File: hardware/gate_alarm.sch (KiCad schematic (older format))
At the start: 8 parts, among them U1 ATtiny212-SS, U2 NodeMCU_1.0_(ESP-12E), U3 NCP718, U4 AH9250

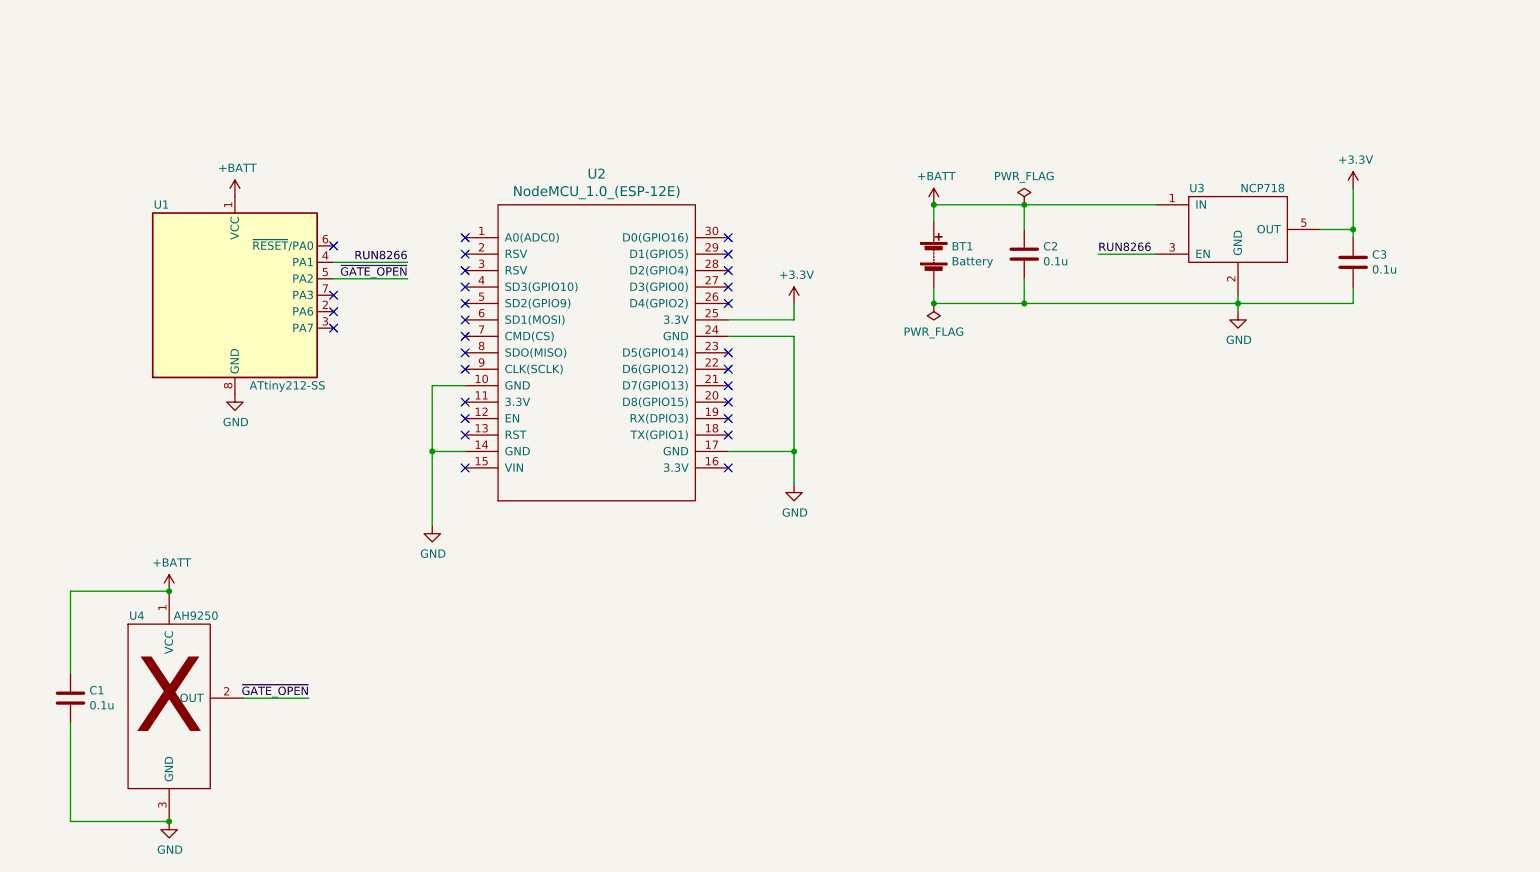
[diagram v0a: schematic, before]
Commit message: Update hardware for first PCB manufacture
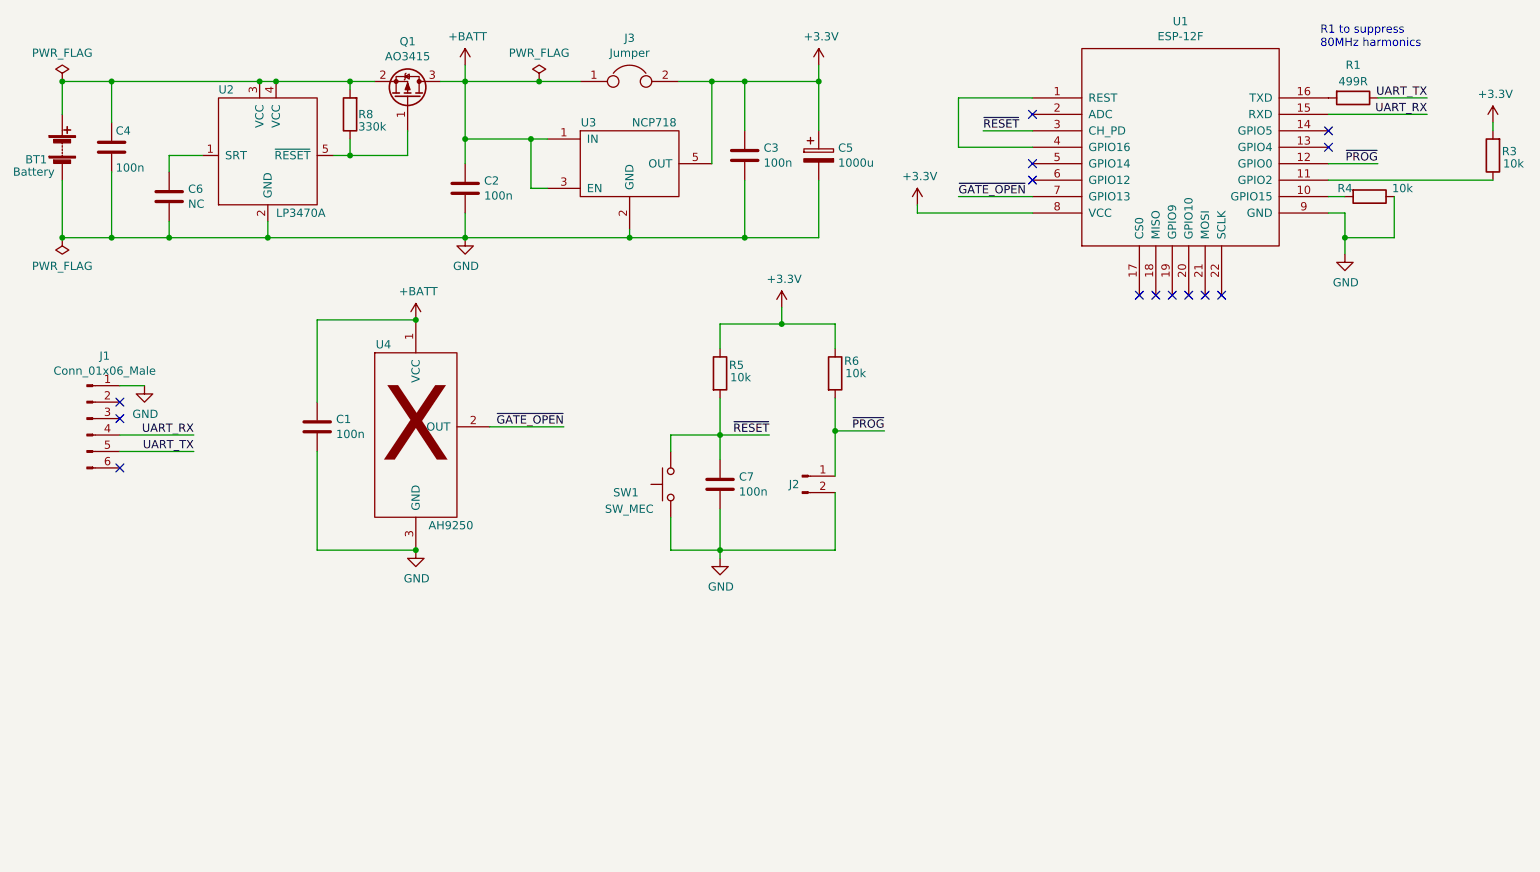
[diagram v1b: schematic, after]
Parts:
- removed U1: ATtiny212-SS, Package_SO:SOIC-8_3.9x4.9mm_P1.27mm, symbol MCU_Microchip_ATtiny:ATtiny212-SS
- removed U2: NodeMCU_1.0_(ESP-12E), ESP8266:NodeMCU1.0(12-E), symbol custom_symbols:NodeMCU_1.0_(ESP-12E)
- added C4, C7: 100n, Capacitors_SMD:C_0805_HandSoldering, symbol Device:C
- added C5: 1000u, Capacitors_THT:CP_Radial_D8.0mm_P3.50mm, symbol Device:CP
- added C6: NC, Capacitors_SMD:C_0805_HandSoldering, symbol Device:C
- added J1: Conn_01x06_Male, Pin_Headers:Pin_Header_Straight_1x06_Pitch2.54mm, symbol Connector:Conn_01x06_Male
- added J2: Conn_01x02_Male, Pin_Headers:Pin_Header_Straight_1x02_Pitch2.54mm, symbol Connector:Conn_01x02_Male
- added J3: Jumper, Jumpers:SolderJumper-2_P1.3mm_Open_Pad1.0x1.5mm, symbol Device:Jumper
- added Q1: AO3415, TO_SOT_Packages_SMD:SOT-23_Handsoldering, symbol Device:Q_PMOS_GSD
- added R1: 499R, Resistors_SMD:R_0805_HandSoldering, symbol Device:R
- added R3, R4, R5, R6: 10k, Resistors_SMD:R_0805_HandSoldering, symbol Device:R
- added R8: 330k, Resistors_SMD:R_0805_HandSoldering, symbol Device:R
- added SW1: SW_MEC, custom_switches:PTS636_THT, symbol custom_switches:SW_MEC
- added U1: ESP-12F, ESP8266:ESP-12E_SMD, symbol ESP8266:ESP-12F
- added U2: LP3470A, TO_SOT_Packages_SMD:SOT-23-5_HandSoldering, symbol power_ics:LP3470A
- C1, C2, C3: value 0.1u -> 100n
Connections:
- net RUN8266 is gone; now on net +BATT: U3.3 (EN)
- net +3V3: now also C5.1, J3.2, R3.2, R5.1, R6.1, U1.8 (VCC)
- net +BATT: now also J3.1, Q1.3 (D); no longer BT1.1 (+)
- net GND: now also C4.2, C5.2, C6.2, C7.2, J1.1 (Pin_1), J2.2 (Pin_2), R4.1, SW1.1 (A), U1.9 (GND), U2.2 (GND)
- net ~GATE_OPEN: now also U1.7 (GPIO13)
- new net: BT1.1 (+), C4.1, Q1.2 (S), R8.2, U2.3 (VCC), U2.4 (VCC)
- new net: Q1.1 (G), R8.1, U2.5 (~RESET)
- new net: U1.1 (REST), U1.4 (GPIO16)
- new net: R4.2, U1.10 (GPIO15)
- new net: R3.1, U1.11 (GPIO2)
- new net: R1.2, U1.16 (TXD)
- new net: C6.1, U2.1 (SRT)
- new net UART_RX: J1.4 (Pin_4), U1.15 (RXD)
- new net UART_TX: J1.5 (Pin_5), R1.1
- new net ~PROG: J2.1 (Pin_1), R6.2, U1.12 (GPIO0)
- new net ~RESET: C7.1, R5.2, SW1.2 (B), U1.3 (CH_PD)
- no-connect marks 29 -> 14
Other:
- note added: "R1 to suppress \n80MHz harmonics"
